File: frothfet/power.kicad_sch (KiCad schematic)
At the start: 46 parts, among them J2 Screw_Terminal_01x08, J3 Screw_Terminal_01x08, U26 TPS7A2033PDBVR, U27 XL1509-5.0, U28 MCP3425A0T-ECH, U29 MAX40200AUK

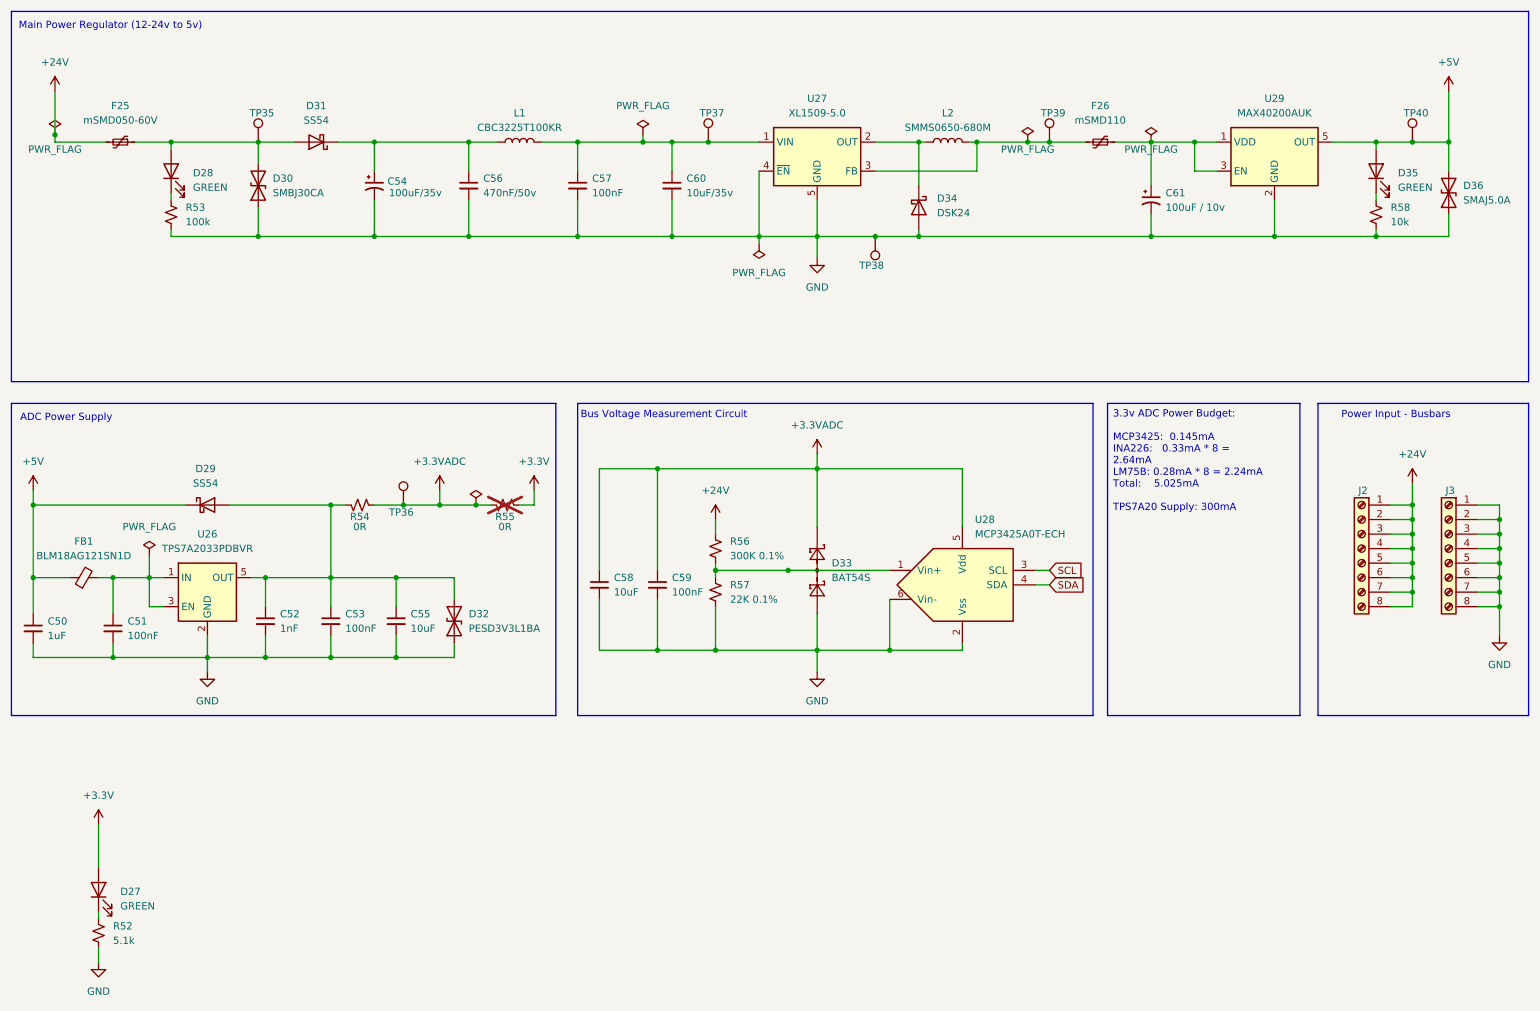
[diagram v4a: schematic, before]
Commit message: tidied up the power schematic a little bit.
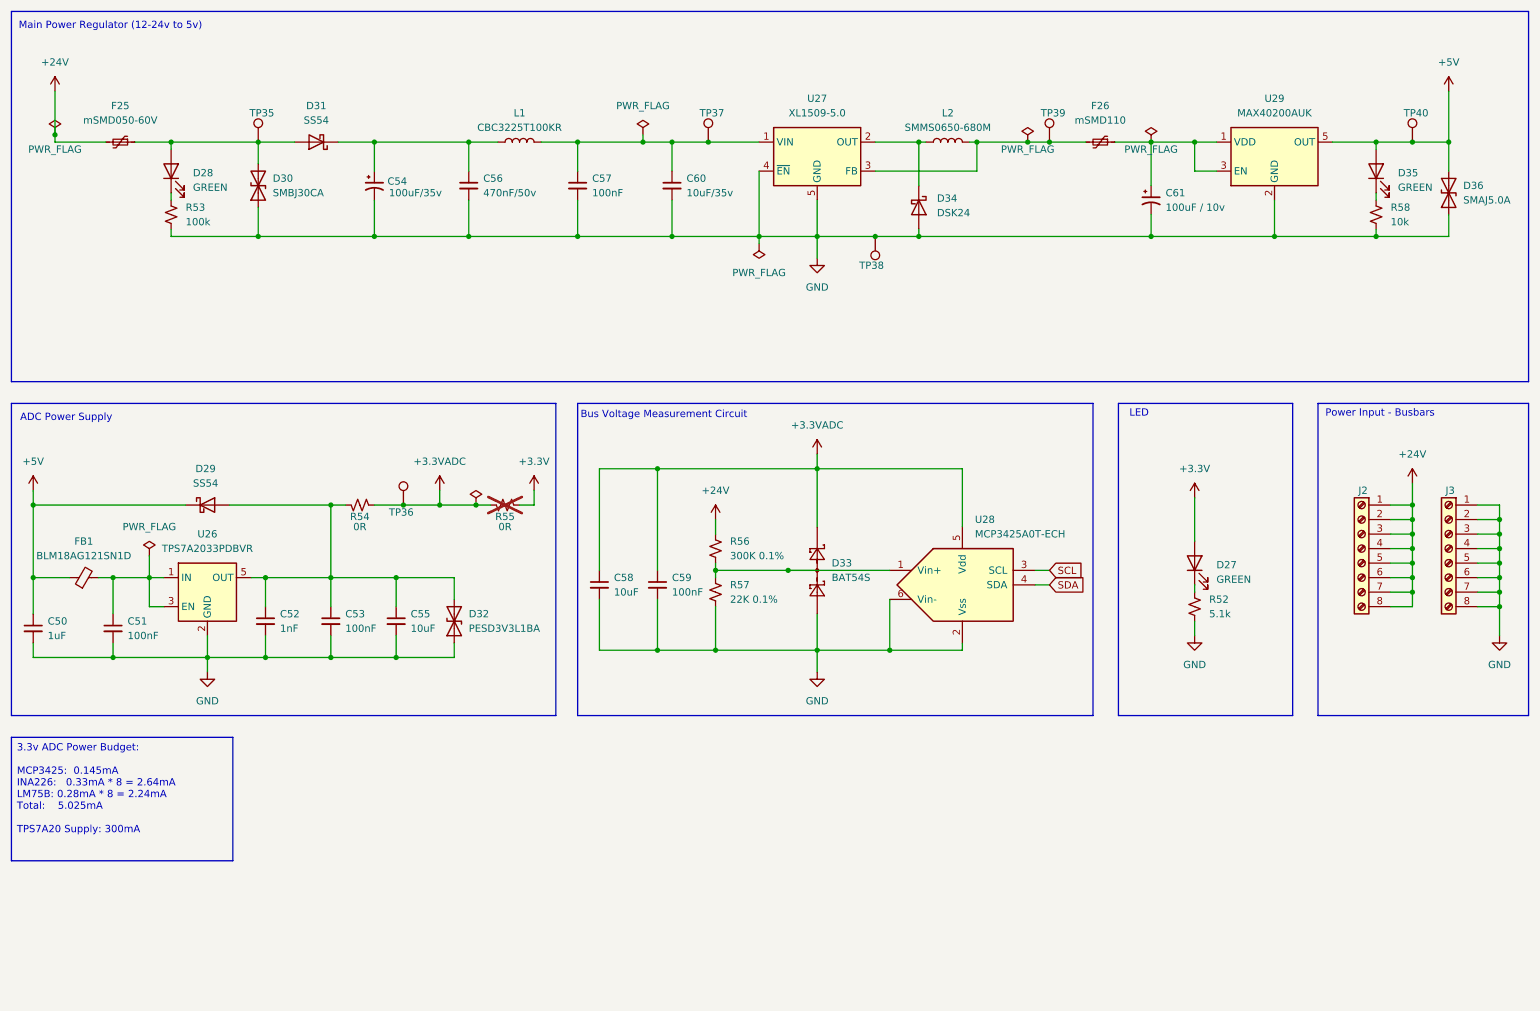
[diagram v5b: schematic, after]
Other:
- note added: "LED"
- moved on the sheet: D27, R52
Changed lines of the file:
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@@
 		)
 	)
+	(rectangle
+		(start 208.915 83.82)
+		(end 239.395 138.43)
+		(stroke
+			(width 0)
+			(type default)
+		)
+		(fill
+			(type none)
+		)
+	)
+	(text "LED"
+		(exclude_from_sim no)
+		(at 210.82 86.36 0)
+		(effects
+			(font
+				(size 1.27 1.27)
+			)
+			(justify left bottom)
+		)
+	)
 	(text "ADC Power Supply"
 		(exclude_from_sim no)
@@
 	(text "Power Input - Busbars"
 		(exclude_from_sim no)
-		(at 247.904 86.614 0)
+		(at 245.11 86.36 0)
 		(effects
 			(font
@@
 	(text_box "3.3v ADC Power Budget:\n\nMCP3425:  0.145mA\nINA226:   0.33mA * 8 = 2.64mA\nLM75B: 0.28mA * 8 = 2.24mA\nTotal:    5.025mA\n\nTPS7A20 Supply: 300mA"
 		(exclude_from_sim no)
-		(at 207.01 83.82 0)
-		(size 33.655 54.61)
+		(at 15.24 142.24 0)
+		(size 38.735 21.59)
 		(margins 0.9525 0.9525 0.9525 0.9525)
 		(stroke
@@
 	(wire
 		(pts
-			(xy 30.48 179.07) (xy 30.48 181.61)
+			(xy 222.25 121.92) (xy 222.25 124.46)
 		)
 		(stroke
@@
 	(wire
 		(pts
-			(xy 30.48 157.48) (xy 30.48 165.1)
+			(xy 222.25 100.33) (xy 222.25 107.95)
 		)
 		(stroke
@@
 	(wire
 		(pts
-			(xy 30.48 172.72) (xy 30.48 173.99)
+			(xy 222.25 115.57) (xy 222.25 116.84)
 		)
 		(stroke
@@
 	(symbol
 		(lib_id "power:+3.3V")
-		(at 30.48 157.48 0)
+		(at 222.25 100.33 0)
 		(unit 1)
 		(exclude_from_sim no)
@@
 		(fields_autoplaced yes)
 		(property "Reference" "#PWR0133"
-			(at 30.48 161.29 0)
+			(at 222.25 104.14 0)
 			(effects
 				(font
@@
 		)
 		(property "Value" "+3.3V"
-			(at 30.48 152.4 0)
+			(at 222.25 95.25 0)
 			(effects
 				(font
@@
 		)
 		(property "Footprint" ""
-			(at 30.48 157.48 0)
+			(at 222.25 100.33 0)
 			(effects
 				(font
@@
 		)
 		(property "Datasheet" ""
-			(at 30.48 157.48 0)
+			(at 222.25 100.33 0)
 			(effects
 				(font
@@
 		)
 		(property "Description" "Power symbol creates a global label with name \"+3.3V\""
-			(at 30.48 157.48 0)
+			(at 222.25 100.33 0)
 			(effects
 				(font
@@
 	(symbol
 		(lib_id "Device:LED")
-		(at 30.48 168.91 90)
+		(at 222.25 111.76 90)
 		(unit 1)
 		(exclude_from_sim no)
@@
 		(fields_autoplaced yes)
 		(property "Reference" "D27"
-			(at 34.29 169.2274 90)
+			(at 226.06 112.0774 90)
 			(effects
 				(font
@@
 		)
 		(property "Value" "GREEN"
-			(at 34.29 171.7674 90)
+			(at 226.06 114.6174 90)
 			(effects
 				(font
@@
 		)
 		(property "Footprint" "LED_SMD:LED_0603_1608Metric"
-			(at 30.48 168.91 0)
+			(at 222.25 111.76 0)
 			(effects
 				(font
@@
 		)
 		(property "Datasheet" "~"
-			(at 30.48 168.91 0)
+			(at 222.25 111.76 0)
 			(effects
 				(font
@@
 		)
 		(property "Description" "Light emitting diode"
-			(at 30.48 168.91 0)
+			(at 222.25 111.76 0)
 			(effects
 				(font
@@
 		)
 		(property "Sim.Pins" "1=K 2=A"
-			(at 30.48 168.91 0)
+			(at 222.25 111.76 0)
 			(effects
 				(font
@@
 		)
 		(property "LCSC" ""
-			(at 30.48 168.91 90)
+			(at 222.25 111.76 90)
 			(effects
 				(font
@@
 	(symbol
 		(lib_id "power:GND")
-		(at 30.48 181.61 0)
+		(at 222.25 124.46 0)
 		(unit 1)
 		(exclude_from_sim no)
@@
 		(fields_autoplaced yes)
 		(property "Reference" "#PWR0134"
-			(at 30.48 187.96 0)
+			(at 222.25 130.81 0)
 			(effects
 				(font
@@
 		)
 		(property "Value" "GND"
-			(at 30.48 186.69 0)
+			(at 222.25 129.54 0)
 			(effects
 				(font
@@
 		)
 		(property "Footprint" ""
-			(at 30.48 181.61 0)
+			(at 222.25 124.46 0)
 			(effects
 				(font
@@
 		)
 		(property "Datasheet" ""
-			(at 30.48 181.61 0)
+			(at 222.25 124.46 0)
 			(effects
 				(font
@@
 		)
 		(property "Description" "Power symbol creates a global label with name \"GND\" , ground"
-			(at 30.48 181.61 0)
+			(at 222.25 124.46 0)
 			(effects
 				(font
@@
 	(symbol
 		(lib_id "Device:R_Small_US")
-		(at 30.48 176.53 0)
+		(at 222.25 119.38 0)
 		(unit 1)
 		(exclude_from_sim no)
@@
 		(fields_autoplaced yes)
 		(property "Reference" "R52"
-			(at 33.02 175.2599 0)
+			(at 224.79 118.1099 0)
 			(effects
 				(font
@@
 		)
 		(property "Value" "5.1k"
-			(at 33.02 177.7999 0)
+			(at 224.79 120.6499 0)
 			(effects
 				(font
@@
 		)
 		(property "Footprint" "Resistor_SMD:R_0603_1608Metric"
-			(at 30.48 176.53 0)
+			(at 222.25 119.38 0)
 			(effects
 				(font
@@
 		)
 		(property "Datasheet" "~"
-			(at 30.48 176.53 0)
+			(at 222.25 119.38 0)
 			(effects
 				(font
@@
 		)
 		(property "Description" "Resistor, small US symbol"
-			(at 30.48 176.53 0)
+			(at 222.25 119.38 0)
 			(effects
 				(font
